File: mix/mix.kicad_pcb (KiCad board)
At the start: 2 copper layers, 35 x 128.5 mm, 30 parts, among them J1 AudioJack2, J2 AudioJack2, J26 WEEE, J27 OSHW, J3 AudioJack2, J4 AudioJack2, J5 AudioJack2, J6 Conn_02x05_Odd_Even, U1 TL072

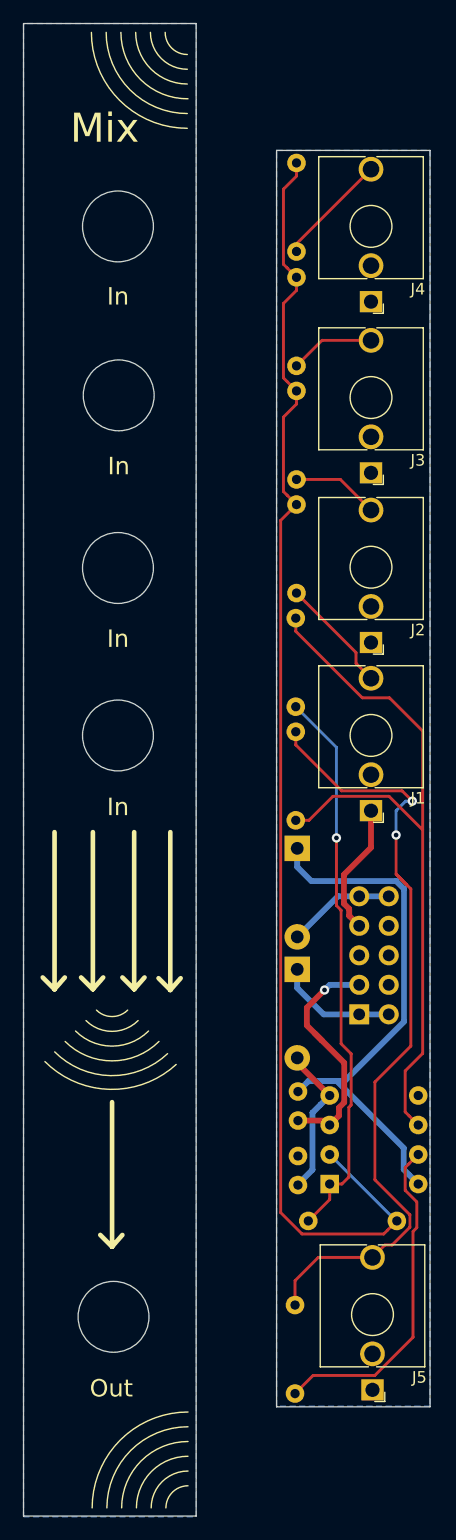
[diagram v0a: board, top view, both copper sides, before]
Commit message: Updating mix to Kicad 9
Swapping out Audiojack2 symbol as it was not present in 9
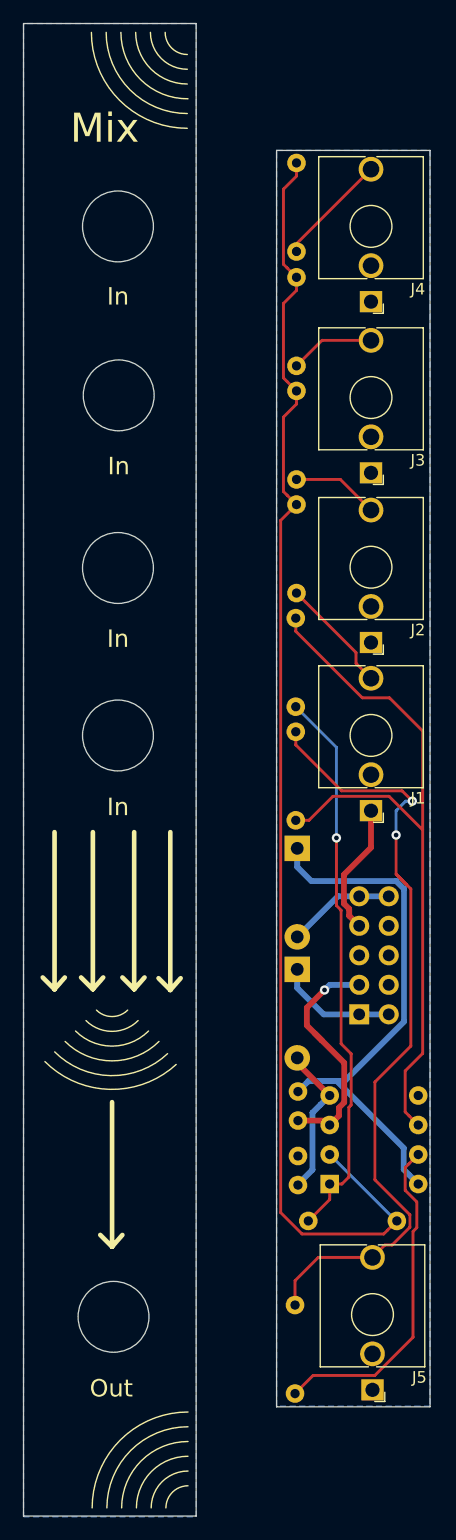
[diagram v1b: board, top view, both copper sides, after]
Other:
- net class Default removed
- net class Power removed
